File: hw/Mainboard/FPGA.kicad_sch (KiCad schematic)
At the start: 46 parts, among them J19 PROG, J21 FPGA-P4, J23 FPGA_P2, J24 FPGA_P3, Q4 MMBT3904, SW5 CONFIG, U21 T8Q144C3, X1 50 MHz

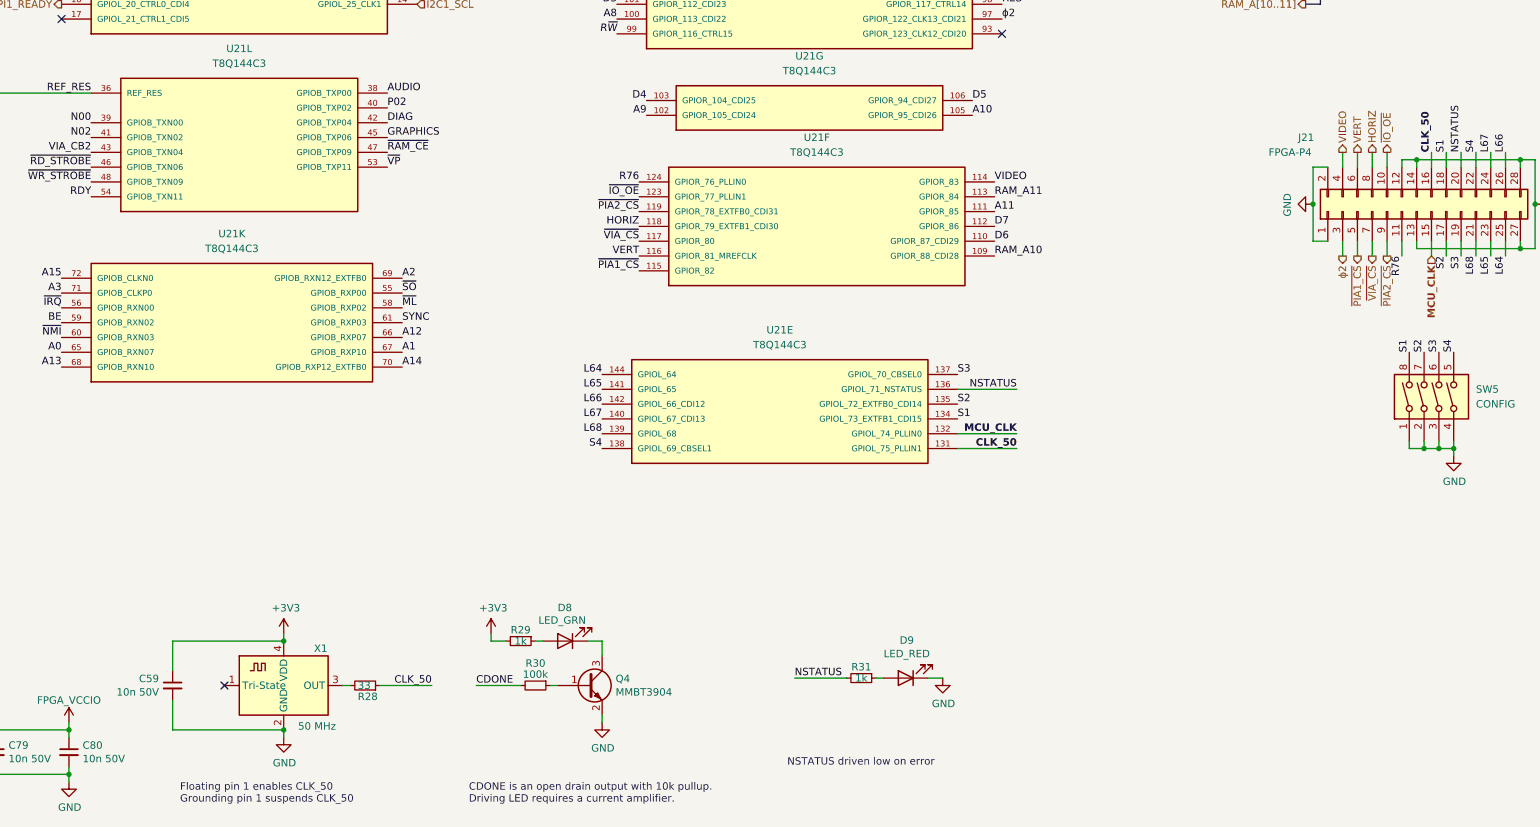
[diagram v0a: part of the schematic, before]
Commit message: hw: remove 50 MHz oscillator
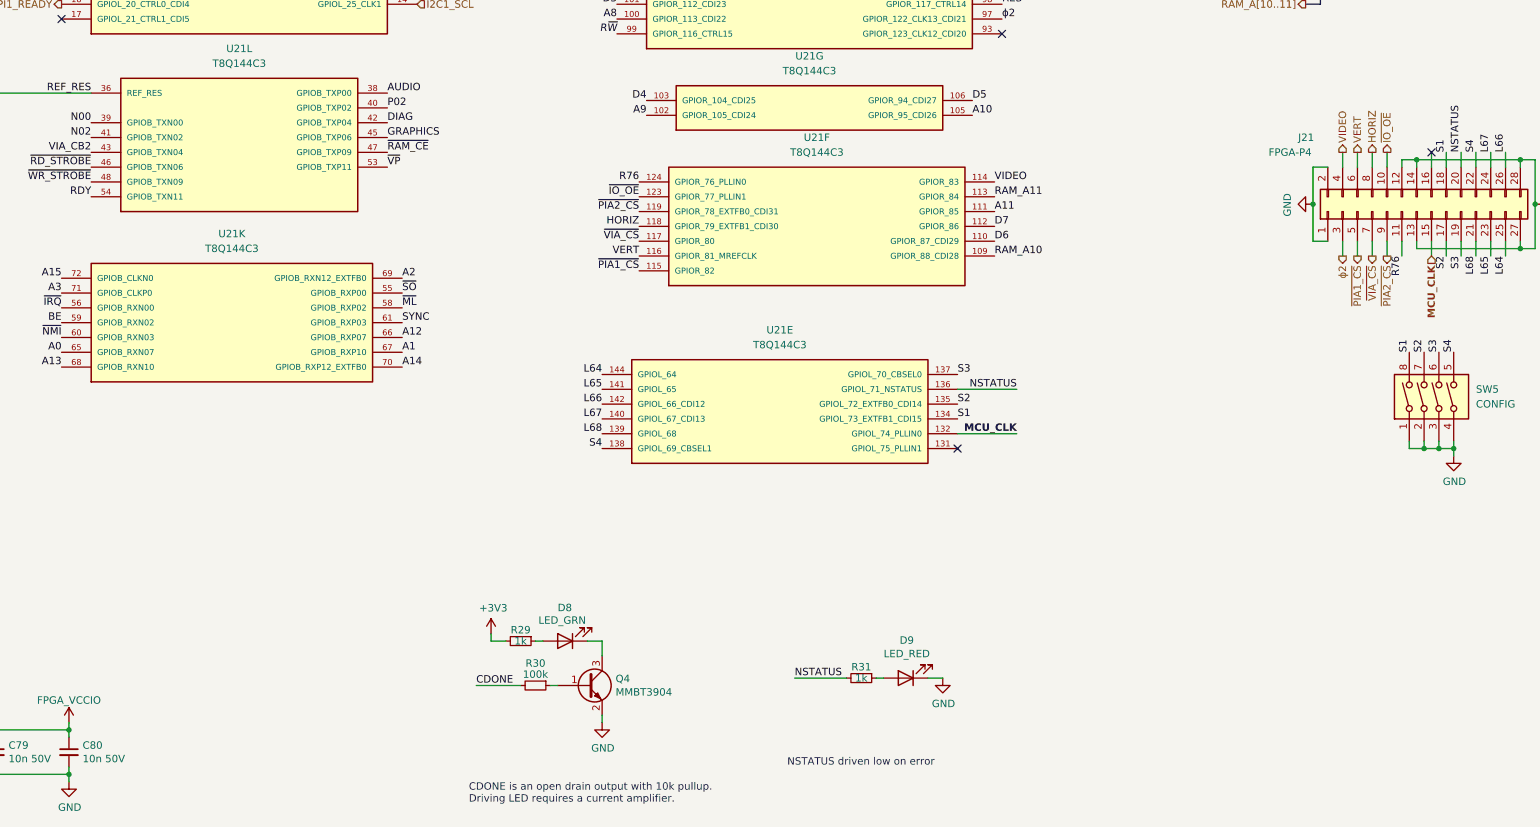
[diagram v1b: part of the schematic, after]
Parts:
- removed C59: 10n 50V, Capacitor_SMD:C_0402_1005Metric, symbol Device:C_Small
- removed R28: 33, Resistor_SMD:R_0402_1005Metric, symbol Device:R_Small
- removed X1: 50 MHz, Crystal:Crystal_SMD_3225-4Pin_3.2x2.5mm, symbol Oscillator:ASCO
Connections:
- net CLK_50: no longer names the net of J21.16 (Pin_16)
- net CLK_50: no longer U21.131 (GPIOL_75_PLLIN1)
- no-connect marks 18 -> 19
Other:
- note removed: "Floating pin 1 enables CLK_50 Grounding pin 1 suspends CLK_50"

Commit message: hw: tidy power and resize pages
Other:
- title: (none) -> CBM PET Mainboard Replacement
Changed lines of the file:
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@@
 (kicad_sch (version 20211123) (generator eeschema)
-  (paper "B")
+  (paper "A")
+  (title_block
+    (title "CBM PET Mainboard Replacement")
+  )
   (junction (at 82.55 233.68) (diameter 0) (color 0 0 0 0)
   )
@@
   (symbol (lib_id "power:GND") (at 364.49 161.29 270) (unit 1)
     (in_bom yes) (on_board yes)
-    (property "Reference" "#PWR?" (id 0) (at 358.14 161.29 0)
+    (property "Reference" "#PWR048" (id 0) (at 358.14 161.29 0)
       (effects (font (size 1.27 1.27)) hide)
     )
@@
   (symbol (lib_id "power:GND") (at 364.49 58.42 270) (unit 1)
     (in_bom yes) (on_board yes)
-    (property "Reference" "#PWR?" (id 0) (at 358.14 58.42 0)
+    (property "Reference" "#PWR034" (id 0) (at 358.14 58.42 0)
       (effects (font (size 1.27 1.27)) hide)
     )
@@
   (symbol (lib_id "power:GND") (at 151.13 260.35 0) (unit 1)
     (in_bom yes) (on_board yes)
-    (property "Reference" "#PWR?" (id 0) (at 151.13 266.7 0)
+    (property "Reference" "#PWR069" (id 0) (at 151.13 266.7 0)
       (effects (font (size 1.27 1.27)) hide)
     )
@@
   (symbol (lib_id "power:+3V3") (at 163.83 30.48 0) (unit 1)
     (in_bom yes) (on_board yes)
-    (property "Reference" "#PWR?" (id 0) (at 163.83 34.29 0)
+    (property "Reference" "#PWR032" (id 0) (at 163.83 34.29 0)
       (effects (font (size 1.27 1.27)) hide)
     )
@@
   (symbol (lib_id "power:+3V3") (at 223.52 234.95 0) (unit 1)
     (in_bom yes) (on_board yes)
-    (property "Reference" "#PWR?" (id 0) (at 223.52 238.76 0)
+    (property "Reference" "#PWR055" (id 0) (at 223.52 238.76 0)
       (effects (font (size 1.27 1.27)) hide)
     )
@@
   (symbol (lib_id "power:GND") (at 388.62 204.47 0) (unit 1)
     (in_bom yes) (on_board yes)
-    (property "Reference" "#PWR?" (id 0) (at 388.62 210.82 0)
+    (property "Reference" "#PWR052" (id 0) (at 388.62 210.82 0)
       (effects (font (size 1.27 1.27)) hide)
     )
@@
   (symbol (lib_id "power:GND") (at 19.05 242.57 0) (unit 1)
     (in_bom yes) (on_board yes)
-    (property "Reference" "#PWR?" (id 0) (at 19.05 248.92 0)
+    (property "Reference" "#PWR056" (id 0) (at 19.05 248.92 0)
       (effects (font (size 1.27 1.27)) hide)
     )
@@
   (symbol (lib_id "PET:FPGA_VCCA") (at 52.07 149.86 0) (unit 1)
     (in_bom yes) (on_board yes) (fields_autoplaced)
-    (property "Reference" "#PWR?" (id 0) (at 52.07 153.67 0)
+    (property "Reference" "#PWR043" (id 0) (at 52.07 153.67 0)
       (effects (font (size 1.27 1.27)) hide)
     )
@@
   (symbol (lib_id "power:+1V2") (at 105.41 143.51 0) (unit 1)
     (in_bom yes) (on_board yes) (fields_autoplaced)
-    (property "Reference" "#PWR?" (id 0) (at 105.41 147.32 0)
+    (property "Reference" "#PWR042" (id 0) (at 105.41 147.32 0)
       (effects (font (size 1.27 1.27)) hide)
     )
@@
   (symbol (lib_id "power:+3V3") (at 332.74 72.39 0) (unit 1)
     (in_bom yes) (on_board yes)
-    (property "Reference" "#PWR?" (id 0) (at 332.74 76.2 0)
+    (property "Reference" "#PWR038" (id 0) (at 332.74 76.2 0)
       (effects (font (size 1.27 1.27)) hide)
     )
@@
   (symbol (lib_id "power:GND") (at 300.99 242.57 0) (unit 1)
     (in_bom yes) (on_board yes)
-    (property "Reference" "#PWR?" (id 0) (at 300.99 248.92 0)
+    (property "Reference" "#PWR061" (id 0) (at 300.99 248.92 0)
       (effects (font (size 1.27 1.27)) hide)
     )
@@
   (symbol (lib_id "PET:FPGA_VCC") (at 95.25 143.51 0) (unit 1)
     (in_bom yes) (on_board yes)
-    (property "Reference" "#PWR?" (id 0) (at 95.25 147.32 0)
+    (property "Reference" "#PWR041" (id 0) (at 95.25 147.32 0)
       (effects (font (size 1.27 1.27)) hide)
     )
@@
   (symbol (lib_id "power:+3V3") (at 237.49 78.74 0) (unit 1)
     (in_bom yes) (on_board yes)
-    (property "Reference" "#PWR?" (id 0) (at 237.49 82.55 0)
+    (property "Reference" "#PWR039" (id 0) (at 237.49 82.55 0)
       (effects (font (size 1.27 1.27)) hide)
     )
@@
   (symbol (lib_id "power:GND") (at 402.59 161.29 90) (mirror x) (unit 1)
     (in_bom yes) (on_board yes)
-    (property "Reference" "#PWR?" (id 0) (at 408.94 161.29 0)
+    (property "Reference" "#PWR049" (id 0) (at 408.94 161.29 0)
       (effects (font (size 1.27 1.27)) hide)
     )
@@
   (symbol (lib_id "PET:PD_GND") (at 160.02 62.23 0) (unit 1)
     (in_bom yes) (on_board yes) (fields_autoplaced)
-    (property "Reference" "#PWR?" (id 0) (at 160.02 68.58 0)
+    (property "Reference" "#PWR036" (id 0) (at 160.02 68.58 0)
       (effects (font (size 1.27 1.27)) hide)
     )
@@
   (symbol (lib_id "power:+3V3") (at 72.39 27.94 0) (unit 1)
     (in_bom yes) (on_board yes)
-    (property "Reference" "#PWR?" (id 0) (at 72.39 31.75 0)
+    (property "Reference" "#PWR031" (id 0) (at 72.39 31.75 0)
       (effects (font (size 1.27 1.27)) hide)
     )
@@
   (symbol (lib_id "power:GND") (at 45.72 66.04 0) (mirror y) (unit 1)
     (in_bom yes) (on_board yes) (fields_autoplaced)
-    (property "Reference" "#PWR?" (id 0) (at 45.72 72.39 0)
+    (property "Reference" "#PWR037" (id 0) (at 45.72 72.39 0)
       (effects (font (size 1.27 1.27)) hide)
     )
@@
   (symbol (lib_id "PET:FPGA_VCCIO") (at 52.07 158.75 0) (unit 1)
     (in_bom yes) (on_board yes)
-    (property "Reference" "#PWR?" (id 0) (at 52.07 162.56 0)
+    (property "Reference" "#PWR047" (id 0) (at 52.07 162.56 0)
       (effects (font (size 1.27 1.27)) hide)
     )
@@
   (symbol (lib_id "power:GND") (at 129.54 149.86 0) (unit 1)
     (in_bom yes) (on_board yes)
-    (property "Reference" "#PWR?" (id 0) (at 129.54 156.21 0)
+    (property "Reference" "#PWR044" (id 0) (at 129.54 156.21 0)
       (effects (font (size 1.27 1.27)) hide)
     )
@@
   (symbol (lib_id "PET:FPGA_VCCIO") (at 151.13 250.19 0) (unit 1)
     (in_bom yes) (on_board yes) (fields_autoplaced)
-    (property "Reference" "#PWR?" (id 0) (at 151.13 254 0)
+    (property "Reference" "#PWR062" (id 0) (at 151.13 254 0)
       (effects (font (size 1.27 1.27)) hide)
     )
@@
   (symbol (lib_id "PET:FPGA_GND") (at 95.25 194.31 0) (unit 1)
     (in_bom yes) (on_board yes)
-    (property "Reference" "#PWR?" (id 0) (at 95.25 200.66 0)
+    (property "Reference" "#PWR050" (id 0) (at 95.25 200.66 0)
       (effects (font (size 1.27 1.27)) hide)
     )
@@
   (symbol (lib_id "power:GND") (at 163.83 38.1 0) (unit 1)
     (in_bom yes) (on_board yes)
-    (property "Reference" "#PWR?" (id 0) (at 163.83 44.45 0)
+    (property "Reference" "#PWR033" (id 0) (at 163.83 44.45 0)
       (effects (font (size 1.27 1.27)) hide)
     )
@@
   (symbol (lib_id "PET:PD_3V3") (at 26.67 158.75 0) (unit 1)
     (in_bom yes) (on_board yes) (fields_autoplaced)
-    (property "Reference" "#PWR?" (id 0) (at 26.67 162.56 0)
+    (property "Reference" "#PWR045" (id 0) (at 26.67 162.56 0)
       (effects (font (size 1.27 1.27)) hide)
     )
@@
   (symbol (lib_id "power:+3V3") (at 38.1 158.75 0) (unit 1)
     (in_bom yes) (on_board yes)
-    (property "Reference" "#PWR?" (id 0) (at 38.1 162.56 0)
+    (property "Reference" "#PWR046" (id 0) (at 38.1 162.56 0)
       (effects (font (size 1.27 1.27)) hide)
     )
@@
   (symbol (lib_id "power:GND") (at 242.57 250.19 0) (unit 1)
     (in_bom yes) (on_board yes)
-    (property "Reference" "#PWR?" (id 0) (at 242.57 256.54 0)
+    (property "Reference" "#PWR063" (id 0) (at 242.57 256.54 0)
       (effects (font (size 1.27 1.27)) hide)
     )
@@
   (symbol (lib_id "power:GND") (at 104.14 194.31 0) (unit 1)
     (in_bom yes) (on_board yes)
-    (property "Reference" "#PWR?" (id 0) (at 104.14 200.66 0)
+    (property "Reference" "#PWR051" (id 0) (at 104.14 200.66 0)
       (effects (font (size 1.27 1.27)) hide)
     )
@@
   (symbol (lib_id "PET:FPGA_VCC") (at 19.05 232.41 0) (unit 1)
     (in_bom yes) (on_board yes) (fields_autoplaced)
-    (property "Reference" "#PWR?" (id 0) (at 19.05 236.22 0)
+    (property "Reference" "#PWR053" (id 0) (at 19.05 236.22 0)
       (effects (font (size 1.27 1.27)) hide)
     )
@@
   (symbol (lib_id "power:GND") (at 402.59 58.42 90) (mirror x) (unit 1)
     (in_bom yes) (on_board yes)
-    (property "Reference" "#PWR?" (id 0) (at 408.94 58.42 0)
+    (property "Reference" "#PWR035" (id 0) (at 408.94 58.42 0)
       (effects (font (size 1.27 1.27)) hide)
     )

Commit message: hw: tidy CPU, rename RD/WR strobe to RAM_OE/_WE, debounce switches
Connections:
- net ~{RD_STROBE} renamed ~{RAM_OE}
- net ~{WR_STROBE} renamed ~{RAM_WE}
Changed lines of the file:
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@@
     (effects (font (size 1.27 1.27)) (justify left bottom))
   )
-  (label "~{RD_STROBE}" (at 154.94 154.94 180)
+  (label "~{RAM_OE}" (at 154.94 154.94 180)
     (effects (font (size 1.27 1.27)) (justify right bottom))
   )
@@
     (effects (font (size 1.27 1.27)) (justify left bottom))
   )
-  (label "~{WR_STROBE}" (at 154.94 157.48 180)
+  (label "~{RAM_WE}" (at 154.94 157.48 180)
     (effects (font (size 1.27 1.27)) (justify right bottom))
   )
@@
     (effects (font (size 1.27 1.27)) (justify right))
   )
-  (hierarchical_label "~{RD_STROBE}" (shape output) (at 382.27 52.07 90)
+  (hierarchical_label "~{RAM_OE}" (shape output) (at 382.27 52.07 90)
     (effects (font (size 1.27 1.27)) (justify left))
   )
@@
     (effects (font (size 1.27 1.27)) (justify right))
   )
-  (hierarchical_label "~{WR_STROBE}" (shape output) (at 379.73 52.07 90)
-    (effects (font (size 1.27 1.27)) (justify left))
-  )
+  (hierarchical_label "~{RAM_WE}" (shape output) (at 379.73 52.07 90)
+    (effects (font (size 1.27 1.27)) (justify left))
+  )

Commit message: hw: replace ram_ce with ram_a15
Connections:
- net A16: no longer J24.10 (Pin_10)
- net ~{RAM_CE} renamed RAM_A15
- new net RAM_A16: J24.10 (Pin_10)
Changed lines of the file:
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@@
   (junction (at 69.85 233.68) (diameter 0) (color 0 0 0 0)
+  )
+  (junction (at 365.76 127) (diameter 0) (color 0 0 0 0)
   )
   (junction (at 57.15 241.3) (diameter 0) (color 0 0 0 0)
@@
     (stroke (width 0) (type default) (color 0 0 0 0))
   )
-  (bus_entry (at 397.51 96.52) (size -2.54 2.54)
-    (stroke (width 0) (type default) (color 0 0 0 0))
-  )
   (bus_entry (at 397.51 93.98) (size -2.54 2.54)
     (stroke (width 0) (type default) (color 0 0 0 0))
@@
     (stroke (width 0) (type default) (color 0 0 0 0))
   )
+  (bus_entry (at 414.02 81.28) (size -2.54 -2.54)
+    (stroke (width 0) (type default) (color 0 0 0 0))
+  )
   (bus_entry (at 397.51 121.92) (size -2.54 -2.54)
     (stroke (width 0) (type default) (color 0 0 0 0))
@@
     (stroke (width 0) (type default) (color 0 0 0 0))
   )
+  (bus_entry (at 414.02 101.6) (size -2.54 -2.54)
+    (stroke (width 0) (type default) (color 0 0 0 0))
+  )
   (bus_entry (at 397.51 109.22) (size -2.54 -2.54)
     (stroke (width 0) (type default) (color 0 0 0 0))
@@
     (stroke (width 0) (type default) (color 0 0 0 0))
   )
+  (bus (pts (xy 414.02 127) (xy 365.76 127))
+    (stroke (width 0) (type default) (color 0 0 0 0))
+  )
   (wire (pts (xy 101.6 193.04) (xy 104.14 193.04))
     (stroke (width 0) (type default) (color 0 0 0 0))
@@
     (stroke (width 0) (type default) (color 0 0 0 0))
   )
-  (bus (pts (xy 397.51 121.92) (xy 397.51 124.46))
+  (bus (pts (xy 397.51 121.92) (xy 397.51 123.19))
     (stroke (width 0) (type default) (color 0 0 0 0))
   )
@@
     (stroke (width 0) (type default) (color 0 0 0 0))
   )
+  (wire (pts (xy 389.89 99.06) (xy 411.48 99.06))
+    (stroke (width 0) (type default) (color 0 0 0 0))
+  )
   (wire (pts (xy 123.19 41.91) (xy 140.97 41.91))
     (stroke (width 0) (type default) (color 0 0 0 0))
@@
     (stroke (width 0) (type default) (color 0 0 0 0))
   )
-  (bus (pts (xy 397.51 124.46) (xy 400.05 124.46))
+  (bus (pts (xy 397.51 123.19) (xy 400.05 123.19))
     (stroke (width 0) (type default) (color 0 0 0 0))
   )
@@
     (stroke (width 0) (type default) (color 0 0 0 0))
   )
+  (bus (pts (xy 414.02 101.6) (xy 414.02 127))
+    (stroke (width 0) (type default) (color 0 0 0 0))
+  )
   (bus (pts (xy 397.51 88.9) (xy 397.51 86.36))
     (stroke (width 0) (type default) (color 0 0 0 0))
@@
     (stroke (width 0) (type default) (color 0 0 0 0))
   )
+  (bus (pts (xy 414.02 81.28) (xy 414.02 101.6))
+    (stroke (width 0) (type default) (color 0 0 0 0))
+  )
   (wire (pts (xy 62.23 187.96) (xy 63.5 187.96))
     (stroke (width 0) (type default) (color 0 0 0 0))
@@
     (stroke (width 0) (type default) (color 0 0 0 0))
   )
-  (bus (pts (xy 397.51 96.52) (xy 397.51 93.98))
-    (stroke (width 0) (type default) (color 0 0 0 0))
-  )
   (wire (pts (xy 113.03 252.73) (xy 113.03 251.46))
     (stroke (width 0) (type default) (color 0 0 0 0))
@@
     (stroke (width 0) (type default) (color 0 0 0 0))
   )
+  (wire (pts (xy 382.27 78.74) (xy 382.27 64.77))
+    (stroke (width 0) (type default) (color 0 0 0 0))
+  )
   (wire (pts (xy 125.73 259.08) (xy 113.03 259.08))
     (stroke (width 0) (type default) (color 0 0 0 0))
@@
     (stroke (width 0) (type default) (color 0 0 0 0))
   )
-  (wire (pts (xy 389.89 99.06) (xy 394.97 99.06))
-    (stroke (width 0) (type default) (color 0 0 0 0))
-  )
   (wire (pts (xy 63.5 175.26) (xy 62.23 175.26))
     (stroke (width 0) (type default) (color 0 0 0 0))
@@
   )
   (wire (pts (xy 63.5 251.46) (xy 76.2 251.46))
+    (stroke (width 0) (type default) (color 0 0 0 0))
+  )
+  (wire (pts (xy 411.48 78.74) (xy 382.27 78.74))
     (stroke (width 0) (type default) (color 0 0 0 0))
   )
@@
     (effects (font (size 1.27 1.27)) (justify left bottom))
   )
-  (label "A16" (at 389.89 99.06 0)
+  (label "RAM_A16" (at 389.89 99.06 0)
     (effects (font (size 1.27 1.27)) (justify left bottom))
   )
@@
     (effects (font (size 1.27 1.27)) (justify left bottom))
   )
-  (label "~{RAM_CE}" (at 205.74 152.4 0)
+  (label "RAM_A15" (at 205.74 152.4 0)
     (effects (font (size 1.27 1.27)) (justify left bottom))
   )
@@
   )
   (label "S3" (at 389.89 170.18 270)
+    (effects (font (size 1.27 1.27)) (justify right bottom))
+  )
+  (label "RAM_A15" (at 411.48 78.74 180)
     (effects (font (size 1.27 1.27)) (justify right bottom))
   )
@@
     (effects (font (size 1.27 1.27)) (justify right))
   )
-  (hierarchical_label "A[0..16]" (shape bidirectional) (at 363.22 81.28 180)
+  (hierarchical_label "A[0..15]" (shape bidirectional) (at 363.22 81.28 180)
     (effects (font (size 1.27 1.27)) (justify right))
   )
@@
     (effects (font (size 1.27 1.27)) (justify right))
   )
-  (hierarchical_label "RAM_A[10..11]" (shape output) (at 363.22 127 180)
+  (hierarchical_label "RAM_A" (shape output) (at 363.22 127 180)
     (effects (font (size 1.27 1.27)) (justify right))
   )
@@
     (effects (font (size 1.27 1.27)) (justify left))
   )
-  (hierarchical_label "D[0..7]" (shape bidirectional) (at 400.05 124.46 0)
+  (hierarchical_label "D[0..7]" (shape bidirectional) (at 400.05 123.19 0)
     (effects (font (size 1.27 1.27)) (justify left))
   )
@@
     (effects (font (size 1.27 1.27)) (justify left))
   )
-  (hierarchical_label "~{RAM_CE}" (shape output) (at 382.27 64.77 270)
-    (effects (font (size 1.27 1.27)) (justify right))
-  )
   (hierarchical_label "~{VIA_CS}" (shape output) (at 374.65 170.18 270)
